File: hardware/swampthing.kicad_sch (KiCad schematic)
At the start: 16 parts, among them Q1 2N3904, U1 TL074, U2 TL074

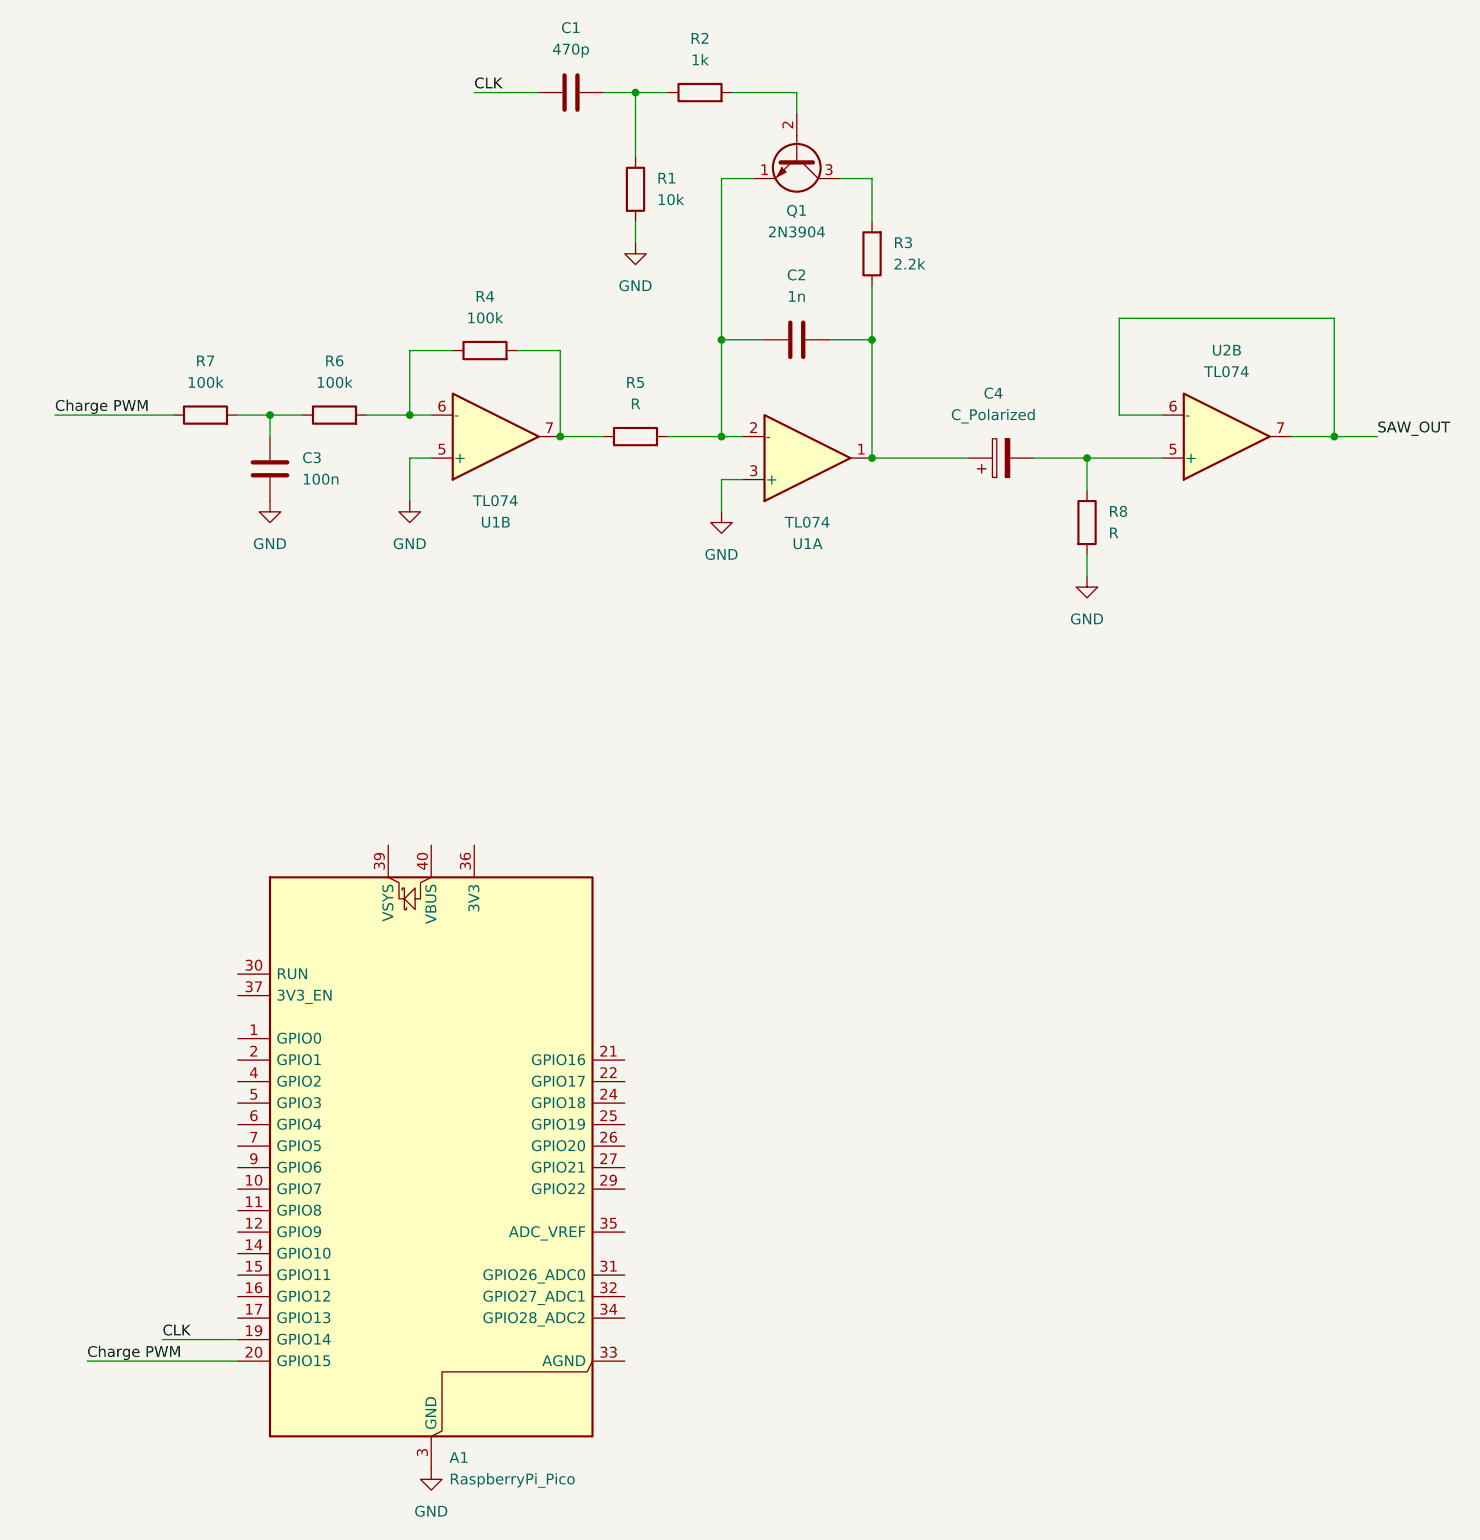
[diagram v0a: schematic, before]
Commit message: Added basic DCO schematic
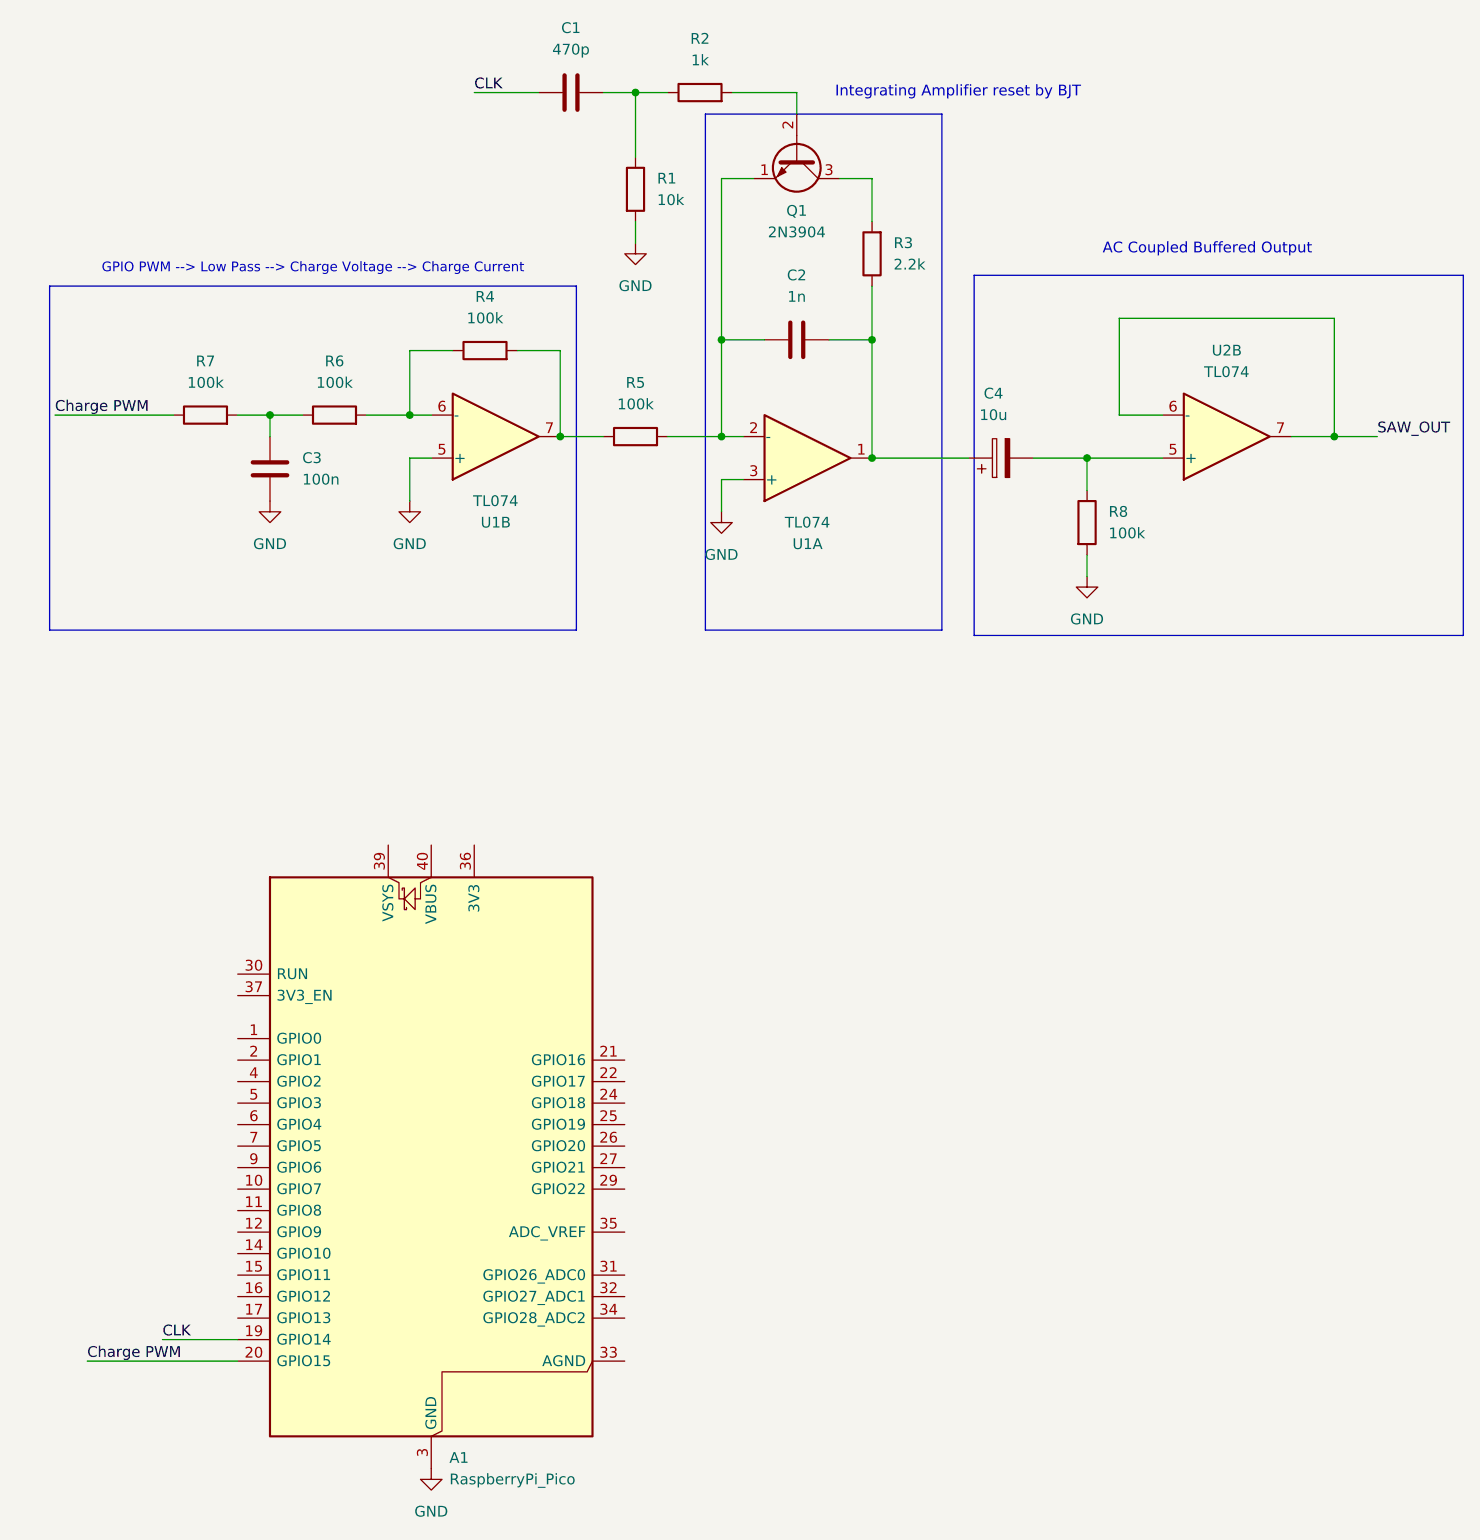
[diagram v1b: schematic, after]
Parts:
- C4: value C_Polarized -> 10u
- R5, R8: value R -> 100k
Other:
- note added: "AC Coupled Buffered Output"
- note added: "GPIO PWM --> Low Pass --> Charge Voltage --> Charge Current"
- note added: "Integrating Amplifier reset by BJT"
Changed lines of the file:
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@@
 	(generator_version "9.0")
 	(paper "A4")
+	(rectangle
+		(start 90.805 27.94)
+		(end 118.745 88.9)
+		(stroke
+			(width 0)
+			(type default)
+		)
+		(fill
+			(type none)
+		)
+	)
+	(rectangle
+		(start 13.335 48.26)
+		(end 75.565 88.9)
+		(stroke
+			(width 0)
+			(type default)
+		)
+		(fill
+			(type none)
+		)
+	)
+	(rectangle
+		(start 122.555 46.99)
+		(end 180.34 89.535)
+		(stroke
+			(width 0)
+			(type default)
+		)
+		(fill
+			(type none)
+		)
+	)
+	(text "Integrating Amplifier reset by BJT"
+		(exclude_from_sim no)
+		(at 120.65 25.4 0)
+		(effects
+			(font
+				(size 1.27 1.27)
+			)
+		)
+	)
+	(text "AC Coupled Buffered Output"
+		(exclude_from_sim no)
+		(at 150.114 43.942 0)
+		(effects
+			(font
+				(size 1.27 1.27)
+			)
+		)
+	)
+	(text "GPIO PWM --> Low Pass --> Charge Voltage --> Charge Current"
+		(exclude_from_sim no)
+		(at 44.45 46.228 0)
+		(effects
+			(font
+				(size 1.143 1.143)
+			)
+		)
+	)
 	(junction
 		(at 110.49 54.61)
@@
 			)
 		)
-		(property "Value" "C_Polarized"
+		(property "Value" "10u"
 			(at 124.841 63.5 90)
 			(effects
@@
 			)
 		)
-		(property "Value" "R"
+		(property "Value" "100k"
 			(at 138.43 77.4699 0)
 			(effects
@@
 			)
 		)
-		(property "Value" "R"
+		(property "Value" "100k"
 			(at 82.55 62.23 90)
 			(effects
